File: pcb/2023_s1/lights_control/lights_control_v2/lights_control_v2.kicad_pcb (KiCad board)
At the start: 2 copper layers, 13 parts

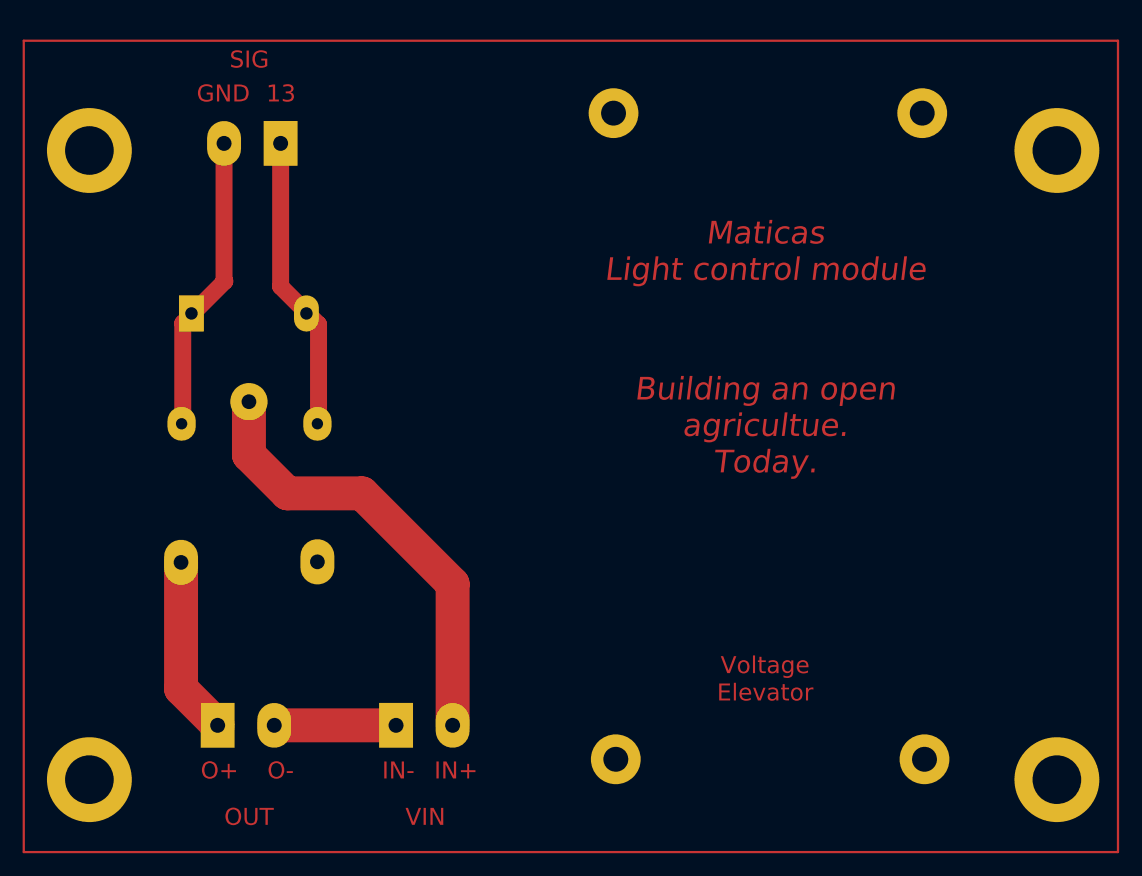
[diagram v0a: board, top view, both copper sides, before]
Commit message: fix, forgot to use 2N2222 as current amplifier of the input signal
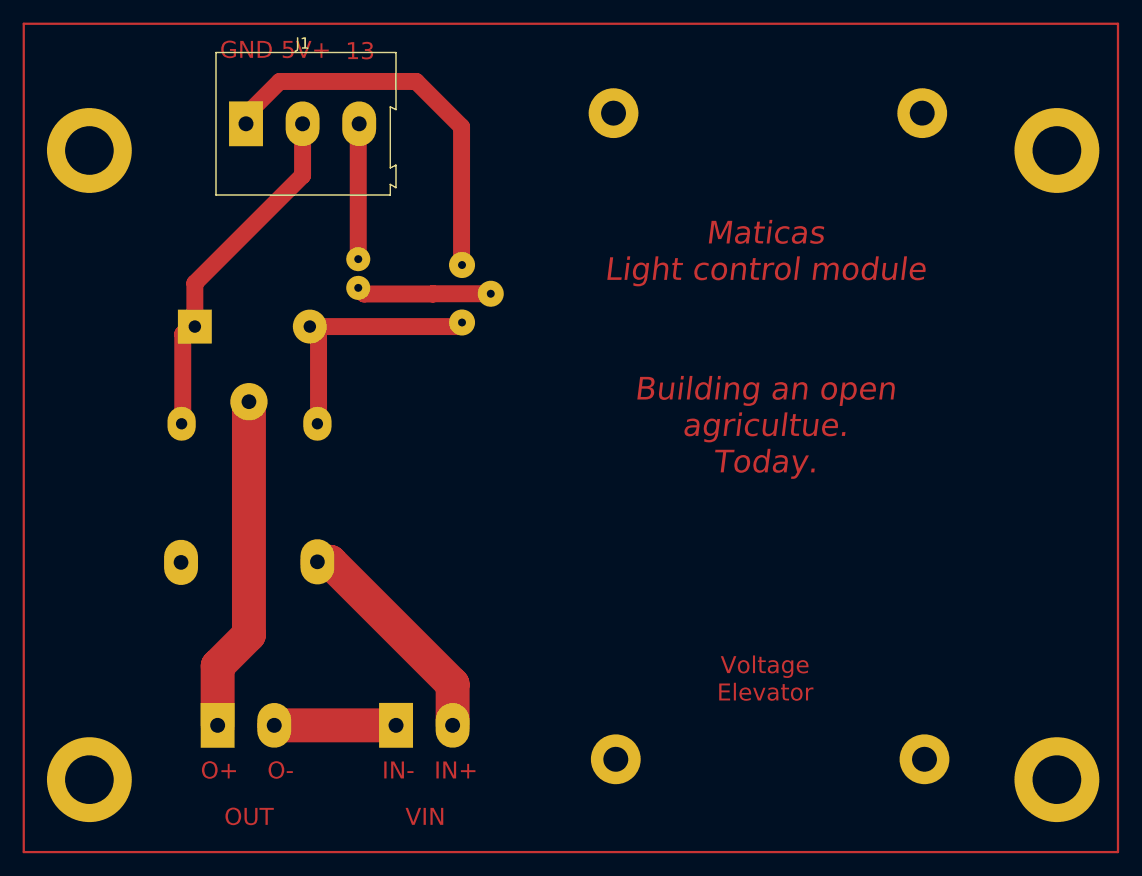
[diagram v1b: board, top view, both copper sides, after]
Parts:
- removed J_IN1: Screw_Terminal_01x02, TerminalBlock:TerminalBlock_Altech_AK300-2_P5.00mm
- added J1: Screw_Terminal_01x03, TerminalBlock:TerminalBlock_Altech_AK300-3_P5.00mm, F.Cu at (112.2, 56.5)
- added Q1: 2N2219, Package_TO_SOT_THT:TO-39-3, B.Cu at (131.3, 69.0)
- added R1: 660, Resistor_THT:R_Axial_DIN0204_L3.6mm_D1.6mm_P2.54mm_Vertical, B.Cu at (122.2, 68.5)
- D1: value 1N4001 -> 1N4004
- moved D1 1.20 mm to (107.7, 74.5)
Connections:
- net 3.3V SIG renamed Net-(K_LIGHTS1-Pad2)
- net GND SIG renamed 5V+
- J_LOAD1 pad 2: LOAD - -> Normally O
- J_LOAD2 pad 1: LOAD + -> LOAD IN
- K_LIGHTS1 pad 1: LOAD - -> LOAD IN
- K_LIGHTS1 pad 3: unconnected-(K_LIGHTS1-Pad3) -> Normally O
- K_LIGHTS1 pad 4: LOAD + -> Normally C
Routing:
- net LOAD -: track 39.9 -> 0.00 mm
- net GND5V: track 0.00 -> 34.9 mm
- net LOAD IN: track 0.00 -> 29.7 mm
- net Normally O: track 0.00 -> 20.1 mm
- net LOAD +: track 15.7 -> 0.00 mm
- net 3.3V SIG: track 0.00 -> 12.0 mm
- net Net-(Q1-Pad2): track 0.00 -> 11.9 mm
- net 5V+: track 26.3 -> 31.1 mm
- net Net-(K_LIGHTS1-Pad2): track 26.2 -> 22.7 mm
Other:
- board text added: "5V+"
- board text removed: "SIG"

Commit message: update
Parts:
- added R2: 50, Resistor_THT:R_Axial_DIN0204_L3.6mm_D1.6mm_P2.54mm_Vertical, B.Cu at (113.4, 67.6)
- moved R1 0.66 mm to (122.2, 67.8)
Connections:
- D1 pad 1: 5V+ -> Net-(D1-Pad1)
- K_LIGHTS1 pad 5: 5V+ -> Net-(D1-Pad1)
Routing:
- net 5V+: track 31.1 -> 12.7 mm
- net Net-(D1-Pad1): track 0.00 -> 16.7 mm
- net 3.3V SIG: track 12.0 -> 11.3 mm
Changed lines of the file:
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@@
   (net 1 "3.3V SIG")
   (net 2 "5V+")
-  (net 3 "Net-(K_LIGHTS1-Pad2)")
+  (net 3 "Net-(D1-Pad1)")
   (net 4 "GND LOAD")
   (net 5 "GND5V")
@@
   (net 8 "Normally C")
   (net 9 "Net-(Q1-Pad2)")
+  (net 10 "Net-(D1-Pad2)")
   (footprint "TerminalBlock:TerminalBlock_Altech_AK300-3_P5.00mm" (layer "F.Cu")
     (at 112.24 56.54)
@@
       (net 9 "Net-(Q1-Pad2)") (pinfunction "B") (pintype "passive"))
     (pad "3" thru_hole oval (at 5.08 0 270) (size 2.3 2.3) (drill 0.7) (layers *.Cu *.Mask)
-      (net 3 "Net-(K_LIGHTS1-Pad2)") (pinfunction "C") (pintype "passive"))
+      (net 10 "Net-(D1-Pad2)") (pinfunction "C") (pintype "passive"))
     (model "${KICAD6_3DMODEL_DIR}/Package_TO_SOT_THT.3dshapes/TO-39-3.wrl"
       (offset (xyz 0 0 0))
@@
       (net 7 "LOAD IN") (pintype "passive"))
     (pad "2" thru_hole oval (at 1.95 -6.05 180) (size 2.5 3) (drill 1) (layers *.Cu *.Mask)
-      (net 3 "Net-(K_LIGHTS1-Pad2)") (pintype "passive"))
+      (net 10 "Net-(D1-Pad2)") (pintype "passive"))
     (pad "3" thru_hole oval (at 14.15 -6.05 180) (size 3 4) (drill 1.3) (layers *.Cu *.Mask)
       (net 6 "Normally O") (pintype "passive"))
@@
       (net 8 "Normally C") (pintype "passive"))
     (pad "5" thru_hole oval (at 1.95 5.95 180) (size 2.5 3) (drill 1) (layers *.Cu *.Mask)
-      (net 2 "5V+") (pintype "passive"))
+      (net 3 "Net-(D1-Pad1)") (pintype "passive"))
     (model "${KICAD6_3DMODEL_DIR}/Relay_THT.3dshapes/Relay_SPDT_SANYOU_SRD_Series_Form_C.wrl"
       (offset (xyz 0 0 0))
@@
     (fp_line (start 2.48 1.35) (end 2.48 -1.35) (layer "B.Fab") (width 0.1))
     (pad "1" thru_hole rect (at 0 0) (size 3 3) (drill 1.1) (layers *.Cu *.Mask)
-      (net 2 "5V+") (pinfunction "K") (pintype "passive"))
+      (net 3 "Net-(D1-Pad1)") (pinfunction "K") (pintype "passive"))
     (pad "2" thru_hole oval (at 10.16 0) (size 3 3) (drill 1.1) (layers *.Cu *.Mask)
-      (net 3 "Net-(K_LIGHTS1-Pad2)") (pinfunction "A") (pintype "passive"))
+      (net 10 "Net-(D1-Pad2)") (pinfunction "A") (pintype "passive"))
     (model "${KICAD6_3DMODEL_DIR}/Diode_THT.3dshapes/D_DO-41_SOD81_P10.16mm_Horizontal.wrl"
       (offset (xyz 0 0 0))
@@
     (pad "1" thru_hole circle (at 0 0 180) (size 7.5 7.5) (drill 4.3) (layers *.Cu *.Mask))
   )
+  (footprint "Resistor_THT:R_Axial_DIN0204_L3.6mm_D1.6mm_P2.54mm_Vertical" (layer "B.Cu")
+    (at 113.4 67.63625 -90)
+    (descr "Resistor, Axial_DIN0204 series, Axial, Vertical, pin pitch=2.54mm, 0.167W, length*diameter=3.6*1.6mm^2, http://cdn-reichelt.de/documents/datenblatt/B400/1_4W%23YAG.pdf")
+    (tags "Resistor Axial_DIN0204 series Axial Vertical pin pitch 2.54mm 0.167W length 3.6mm diameter 1.6mm")
+    (property "Sheetfile" "lights_control_v2.kicad_sch")
+    (property "Sheetname" "")
+    (attr through_hole)
+    (fp_text reference "R2" (at 1.27 1.92 90) (layer "B.SilkS")
+      (effects (font (size 1 1) (thickness 0.15)) (justify mirror))
+    )
+    (fp_text value "50" (at 1.27 -1.92 90) (layer "B.Fab")
+      (effects (font (size 1 1) (thickness 0.15)) (justify mirror))
+    )
+    (fp_text user "${REFERENCE}" (at 1.27 1.92 90) (layer "B.Fab")
+      (effects (font (size 1 1) (thickness 0.15)) (justify mirror))
+    )
+    (fp_line (start 0.92 0) (end 1.54 0) (layer "B.SilkS") (width 0.12))
+    (fp_circle (center 0 0) (end 0.92 0) (layer "B.SilkS") (width 0.12) (fill none))
+    (fp_line (start -1.05 -1.05) (end 3.49 -1.05) (layer "B.CrtYd") (width 0.05))
+    (fp_line (start -1.05 1.05) (end -1.05 -1.05) (layer "B.CrtYd") (width 0.05))
+    (fp_line (start 3.49 -1.05) (end 3.49 1.05) (layer "B.CrtYd") (width 0.05))
+    (fp_line (start 3.49 1.05) (end -1.05 1.05) (layer "B.CrtYd") (width 0.05))
+    (fp_line (start 0 0) (end 2.54 0) (layer "B.Fab") (width 0.1))
+    (fp_circle (center 0 0) (end 0.8 0) (layer "B.Fab") (width 0.1) (fill none))
+    (pad "1" thru_hole circle (at 0 0 270) (size 2.125 2.125) (drill 0.7) (layers *.Cu *.Mask)
+      (net 2 "5V+") (pintype "passive"))
+    (pad "2" thru_hole oval (at 2.54 0 270) (size 2.125 2.125) (drill 0.7) (layers *.Cu *.Mask)
+      (net 3 "Net-(D1-Pad1)") (pintype "passive"))
+    (model "${KICAD6_3DMODEL_DIR}/Resistor_THT.3dshapes/R_Axial_DIN0204_L3.6mm_D1.6mm_P2.54mm_Vertical.wrl"
+      (offset (xyz 0 0 0))
+      (scale (xyz 1 1 1))
+      (rotate (xyz 0 0 0))
+    )
+  )
   (footprint "TerminalBlock:TerminalBlock_Altech_AK300-2_P5.00mm" (layer "B.Cu")
     (at 125.5 109.7)
@@
   )
   (footprint "Resistor_THT:R_Axial_DIN0204_L3.6mm_D1.6mm_P2.54mm_Vertical" (layer "B.Cu")
-    (at 122.16 68.5 -90)
+    (at 122.16 67.83625 -90)
     (descr "Resistor, Axial_DIN0204 series, Axial, Vertical, pin pitch=2.54mm, 0.167W, length*diameter=3.6*1.6mm^2, http://cdn-reichelt.de/documents/datenblatt/B400/1_4W%23YAG.pdf")
     (tags "Resistor Axial_DIN0204 series Axial Vertical pin pitch 2.54mm 0.167W length 3.6mm diameter 1.6mm")
@@
     (effects (font (size 1 1) (thickness 0.15)) (justify mirror))
   )
-  (segment (start 122.16 68.52) (end 122.16 56.62) (width 1.5) (layer "F.Cu") (net 1))
+  (segment (start 122.16 67.83625) (end 122.16 56.62) (width 1.5) (layer "F.Cu") (net 1))
   (segment (start 122.16 56.62) (end 122.24 56.54) (width 1.5) (layer "F.Cu") (net 1))
-  (segment (start 107.72 74.46) (end 107.31 74.46) (width 1.5) (layer "F.Cu") (net 2))
-  (segment (start 106.65 75.12) (end 106.65 83.05) (width 1.5) (layer "F.Cu") (net 2))
-  (segment (start 107.72 70.63) (end 107.72 74.46) (width 1.5) (layer "F.Cu") (net 2))
-  (segment (start 117.24 61.11) (end 107.72 70.63) (width 1.5) (layer "F.Cu") (net 2))
-  (segment (start 107.31 74.46) (end 106.65 75.12) (width 1.5) (layer "F.Cu") (net 2))
-  (segment (start 117.24 56.54) (end 117.24 61.11) (width 1.5) (layer "F.Cu") (net 2))
-  (segment (start 117.69 74.46) (end 118.65 75.42) (width 1.5) (layer "F.Cu") (net 3))
-  (segment (start 130.95 74.46) (end 117.69 74.46) (width 1.5) (layer "F.Cu") (net 3))
-  (segment (start 118.65 75.42) (end 118.65 83.05) (width 1.5) (layer "F.Cu") (net 3))
-  (segment (start 131.29 74.12) (end 130.95 74.46) (width 1.5) (layer "F.Cu") (net 3))
+  (segment (start 113.4 67.63625) (end 113.4 65.9) (width 1.5) (layer "F.Cu") (net 2))
+  (segment (start 113.4 65.9) (end 117.24 62.06) (width 1.5) (layer "F.Cu") (net 2))
+  (segment (start 117.24 62.06) (end 117.24 56.54) (width 1.5) (layer "F.Cu") (net 2))
+  (segment (start 107.72 74.46) (end 107.31 74.46) (width 1.5) (layer "F.Cu") (net 3))
+  (segment (start 113.32375 70.17625) (end 113.4 70.17625) (width 1.5) (layer "F.Cu") (net 3))
+  (segment (start 109.04 74.46) (end 113.32375 70.17625) (width 1.5) (layer "F.Cu") (net 3))
+  (segment (start 106.65 75.12) (end 106.65 83.05) (width 1.5) (layer "F.Cu") (net 3))
+  (segment (start 107.31 74.46) (end 106.65 75.12) (width 1.5) (layer "F.Cu") (net 3))
+  (segment (start 107.72 74.46) (end 109.04 74.46) (width 1.5) (layer "F.Cu") (net 3))
   (segment (start 114.735 109.7) (end 125.5 109.7) (width 3) (layer "F.Cu") (net 4))
   (segment (start 115.22 52.8) (end 112.24 55.78) (width 1.5) (layer "F.Cu") (net 5))
@@
   (segment (start 109.735 104.455) (end 109.735 109.7) (width 3) (layer "F.Cu") (net 7))
   (segment (start 112.5 81.1) (end 112.5 101.69) (width 3) (layer "F.Cu") (net 7))
-  (segment (start 122.68 71.58) (end 122.16 71.06) (width 1.5) (layer "F.Cu") (net 9))
+  (segment (start 128.75 71.58) (end 123.62 71.58) (width 1.5) (layer "F.Cu") (net 9))
   (segment (start 128.77 71.56) (end 133.87 71.56) (width 1.5) (layer "F.Cu") (net 9))
-  (segment (start 128.75 71.58) (end 122.68 71.58) (width 1.5) (layer "F.Cu") (net 9))
   (segment (start 128.75 71.58) (end 128.77 71.56) (width 1.5) (layer "F.Cu") (net 9))
+  (segment (start 123.4 71.61625) (end 122.16 70.37625) (width 1.5) (layer "F.Cu") (net 9))
+  (segment (start 117.69 74.46) (end 118.65 75.42) (width 1.5) (layer "F.Cu") (net 10))
+  (segment (start 130.95 74.46) (end 117.69 74.46) (width 1.5) (layer "F.Cu") (net 10))
+  (segment (start 118.65 75.42) (end 118.65 83.05) (width 1.5) (layer "F.Cu") (net 10))
+  (segment (start 131.29 74.12) (end 130.95 74.46) (width 1.5) (layer "F.Cu") (net 10))
   (group "" (id bc76b15f-4bf7-4f82-a936-af88d40a6eaf)
     (members
